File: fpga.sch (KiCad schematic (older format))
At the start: 67 parts, among them J10 CLK9, J11 CLK8, J12 CLK2, J13 SD_CLK, P1 JTAG_CONN, SW2 SW_PUSH, SW3 SW_PUSH, U10 S25FL216K, U12 TLV70012, U13 TLV70025, U14 TLV70012, U2 EP4CE15E22

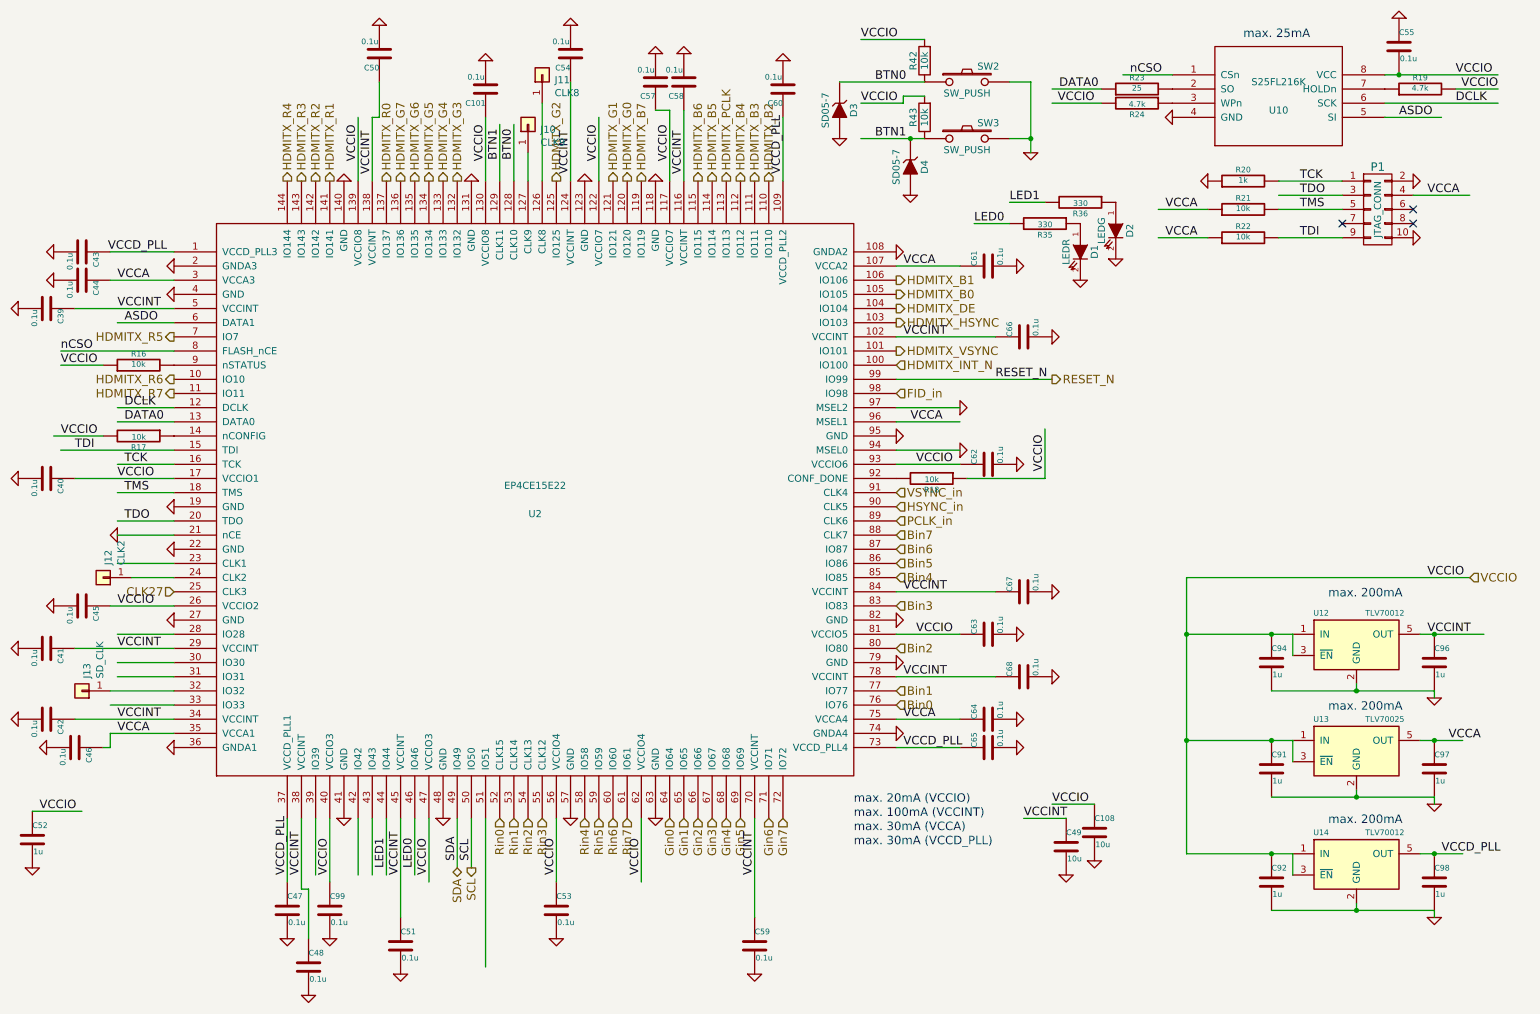
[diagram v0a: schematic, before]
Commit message: NeXT Sound Box function (1st rev) (#1)
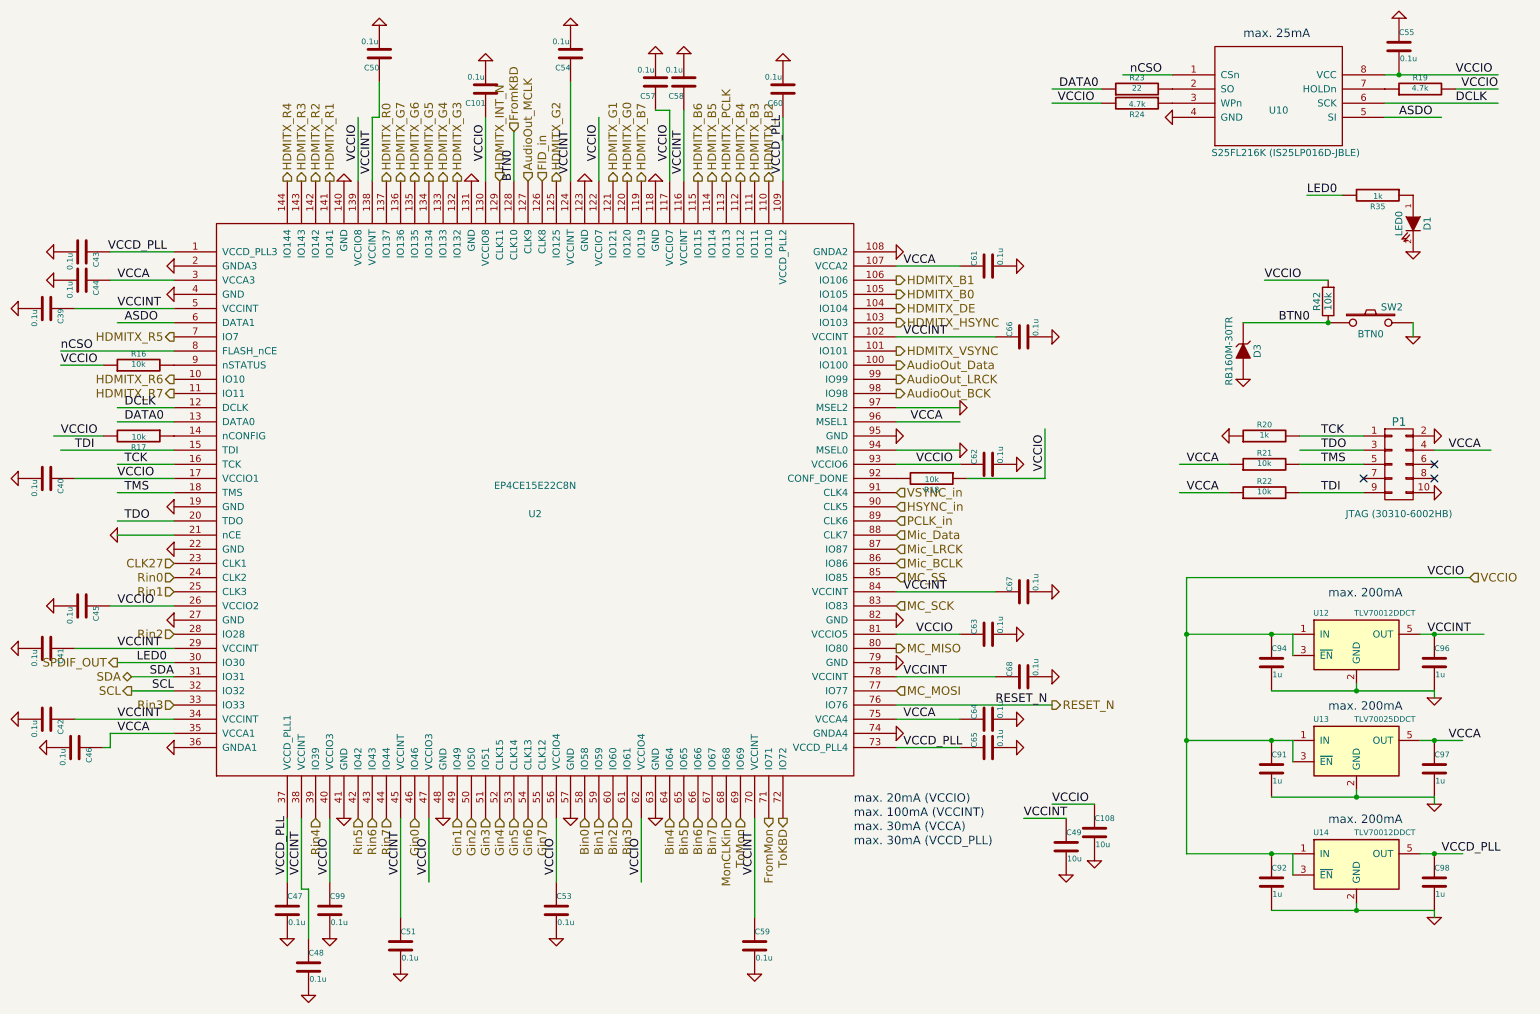
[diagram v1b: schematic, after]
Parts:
- removed C52: 1u, custom_components:SM0603_Capa_libcms, symbol ossc_board-rescue:C-RESCUE-ossc_board
- removed D2: LEDG, custom_components:LED-0603, symbol ossc_board-rescue:LED-RESCUE-ossc_board
- removed D4: SD05-7, custom_components:SOD-323_Handsoldering, symbol ossc_board-rescue:ZENER
- removed J10: CLK9, custom_components:TestPad-D1.0mm, symbol Connector_Generic:Conn_01x01
- removed J11: CLK8, custom_components:TestPad-D1.0mm, symbol Connector_Generic:Conn_01x01
- removed J12: CLK2, custom_components:TestPad-D1.0mm, symbol Connector_Generic:Conn_01x01
- removed J13: SD_CLK, custom_components:TestPad-D1.0mm, symbol Connector_Generic:Conn_01x01
- removed R36: 330, custom_components:SM0603_Resistor_libcms, symbol ossc_board-rescue:R-RESCUE-ossc_board
- removed R43: 10k, custom_components:SM0603_Resistor_libcms, symbol ossc_board-rescue:R
- removed SW3: SW_PUSH, Button_Switch_THT:SW_PUSH_6mm_H5mm, symbol ossc_board-rescue:SW_PUSH
- C101, C108, C39, C40, C41, C42, C43, C44, C45, C46, C47, C48, C49, C50, C51, C53, C54, C55, C57, C58, C59, C60, C61, C62, C63, C64, C65, C66, C67, C68, C91, C92, C94, C96, C97, C98, C99: footprint custom_components:SM0603_Capa_libcms -> Capacitor_SMD:C_0603_1608Metric_Pad1.05x0.95mm_HandSolder
- D1: value LEDR -> LED0; footprint custom_components:LED-0603 -> LED_THT:LED_D3.0mm_Horizontal_O1.27mm_Z6.0mm
- D3: value SD05-7 -> RB160M-30TR; footprint custom_components:SOD-323_Handsoldering -> custom_components:D_SOD-123_HandSoldering
- P1: value JTAG_CONN -> JTAG (30310-6002HB)
- R16, R17, R18, R19, R20, R21, R22, R24, R42: footprint custom_components:SM0603_Resistor_libcms -> Resistor_SMD:R_0603_1608Metric_Pad1.05x0.95mm_HandSolder
- R23: value 25 -> 22; footprint custom_components:SM0603_Resistor_libcms -> Resistor_SMD:R_0603_1608Metric_Pad1.05x0.95mm_HandSolder
- R35: value 330 -> 1k; footprint custom_components:SM0603_Resistor_libcms -> Resistor_SMD:R_0603_1608Metric_Pad1.05x0.95mm_HandSolder
- SW2: value SW_PUSH -> BTN0; footprint Button_Switch_THT:SW_PUSH_6mm_H5mm -> Button_Switch_THT:SW_Tactile_SKHH_Angled
- U10: value S25FL216K -> S25FL216K (IS25LP016D-JBLE)
- U12, U14: value TLV70012 -> TLV70012DDCT
- U13: value TLV70025 -> TLV70025DDCT
- U2: value EP4CE15E22 -> EP4CE15E22C8N
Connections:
- net labels added: AudioOut_BCK, AudioOut_Data, AudioOut_LRCK, AudioOut_MCLK, FromKBD, FromMon, MC_MISO, MC_MOSI, MC_SCK, MC_SS, Mic_BCLK, Mic_Data, Mic_LRCK, MonCLKin, SPDIF_OUT, ToKBD, ToMon
- net labels removed: BTN1, LED1
- wire segments 137 -> 112
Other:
- moved on the sheet: D1, D3, P1, R20, R21, R22, R35, R42, SW2
